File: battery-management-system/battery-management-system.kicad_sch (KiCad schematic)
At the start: 18 parts, among them J1 Conn_01x01

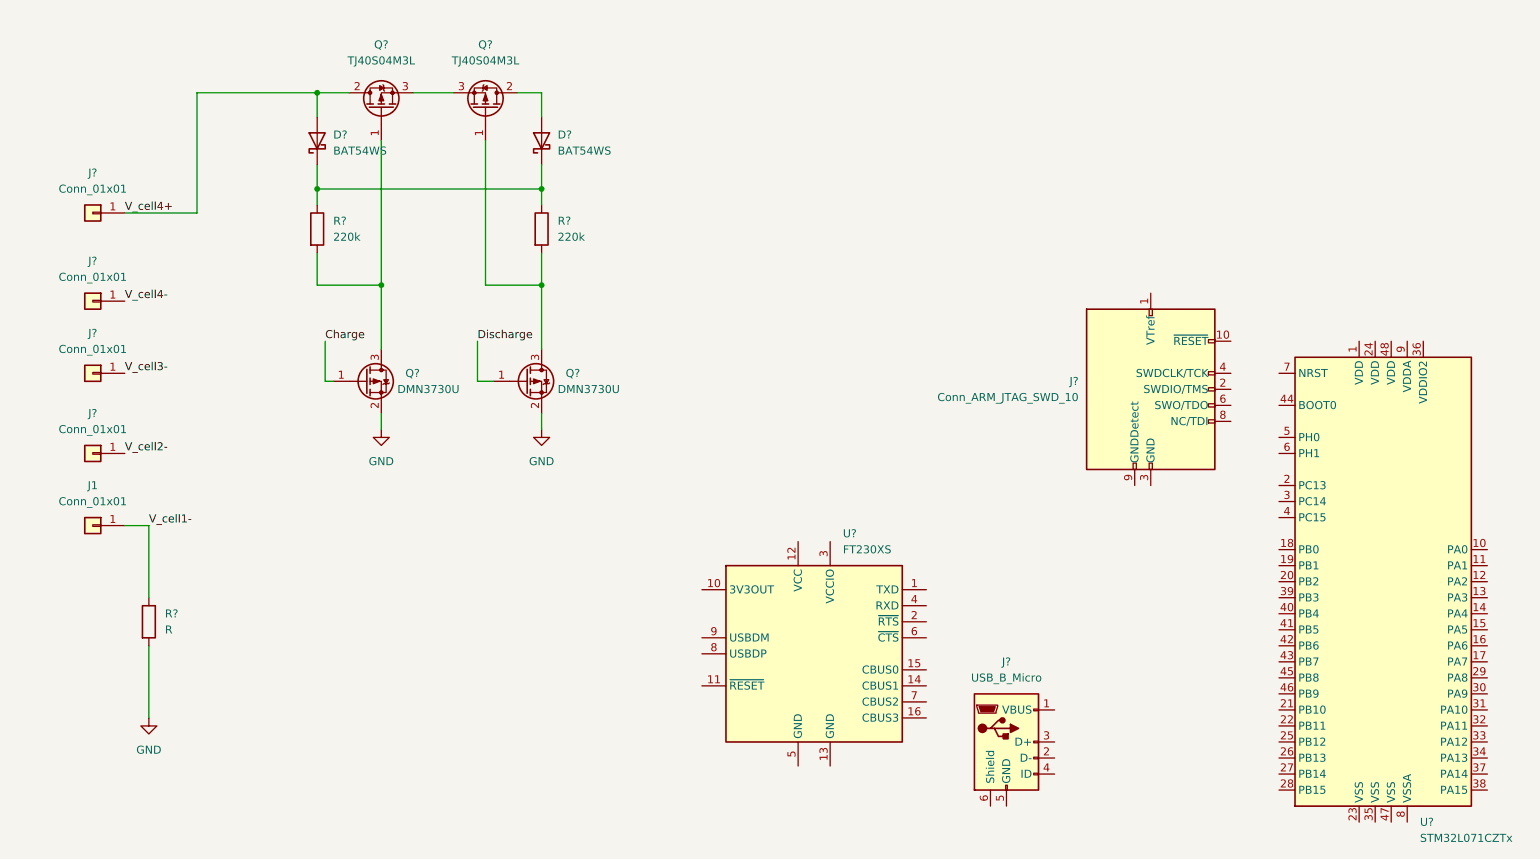
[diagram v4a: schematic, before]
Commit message: introduce hierarchical sheets
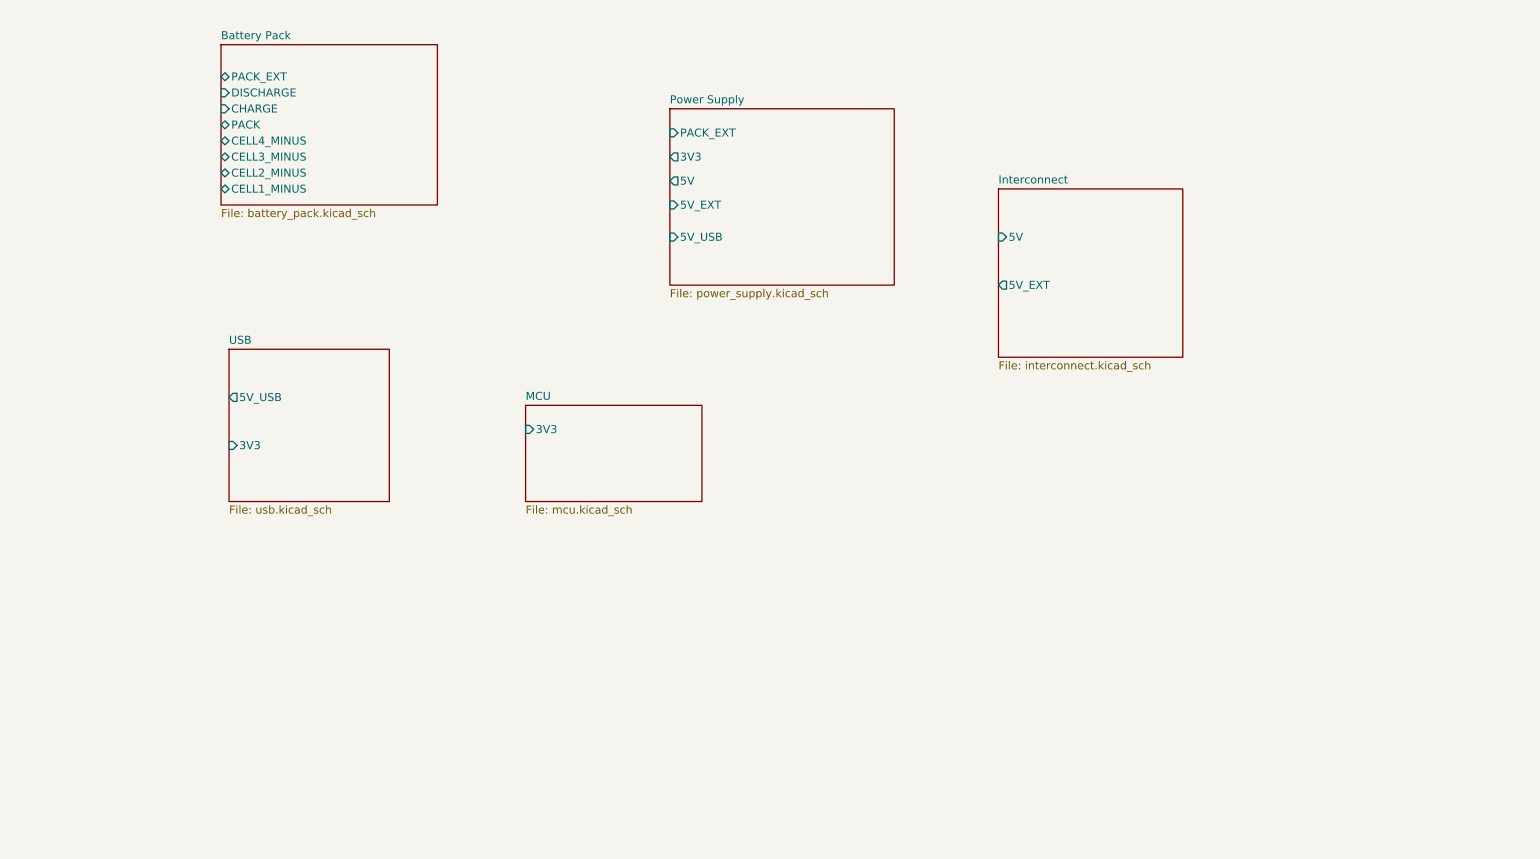
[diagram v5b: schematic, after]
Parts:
- removed D? (x2): BAT54WS, Diode_SMD:D_SOD-323, symbol benediktibk:BAT54WS
- removed J1, J? (x4): Conn_01x01, symbol Connector_Generic:Conn_01x01
- removed J?: USB_B_Micro, symbol Connector:USB_B_Micro
- removed J?: Conn_ARM_JTAG_SWD_10, symbol Connector:Conn_ARM_JTAG_SWD_10
- removed Q? (x2): DMN3730U, Package_TO_SOT_SMD:SOT-23, symbol benediktibk:DMN3730U
- removed Q? (x2): TJ40S04M3L, Package_TO_SOT_SMD:TO-252-2, symbol benediktibk:TJ40S04M3L
- removed R? (x2): 220k, Resistor_SMD:R_0603_1608Metric, symbol Device:R
- removed R?: R, symbol Device:R
- removed U?: STM32L071CZTx, Package_QFP:LQFP-48_7x7mm_P0.5mm, symbol MCU_ST_STM32L0:STM32L071CZTx
- removed U?: FT230XS, Package_SO:SSOP-16_3.9x4.9mm_P0.635mm, symbol Interface_USB:FT230XS
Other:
- added sheet Battery Pack (battery_pack.kicad_sch)
- added sheet Interconnect (interconnect.kicad_sch)
- added sheet MCU (mcu.kicad_sch)
- added sheet Power Supply (power_supply.kicad_sch)
- added sheet USB (usb.kicad_sch)

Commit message: define basic hierarchy and power supplies
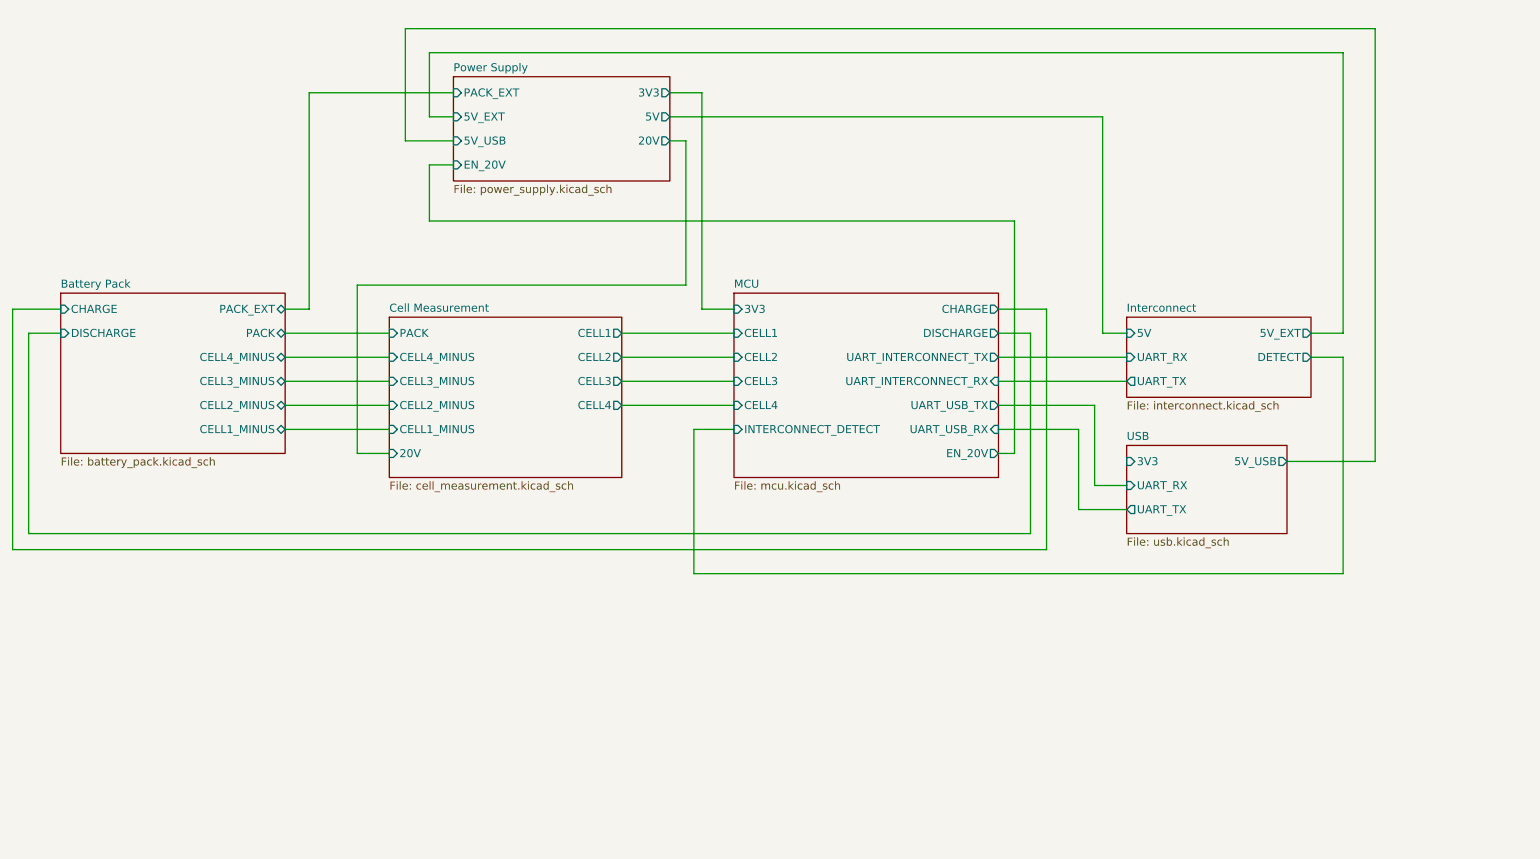
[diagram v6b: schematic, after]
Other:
- added sheet Cell Measurement (cell_measurement.kicad_sch)
- sheet Interconnect ports: added DETECT, UART_RX, UART_TX; removed none
- sheet MCU ports: added CELL1, CELL2, CELL3, CELL4, CHARGE, DISCHARGE, EN_20V, INTERCONNECT_DETECT, UART_INTERCONNECT_RX, UART_INTERCONNECT_TX, UART_USB_RX, UART_USB_TX; removed none
- sheet Power Supply ports: added 20V, EN_20V; removed none
- sheet USB ports: added UART_RX, UART_TX; removed none
